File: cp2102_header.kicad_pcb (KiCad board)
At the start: 2 copper layers, 15.2 x 22.9 mm, 32 parts, among them J1 FTDI, J2 USB_B_Micro, J22 USB_B_Micro, J8 mount, Q3 BSS138PS, Q4 BSS138PS, U2 CP2102N

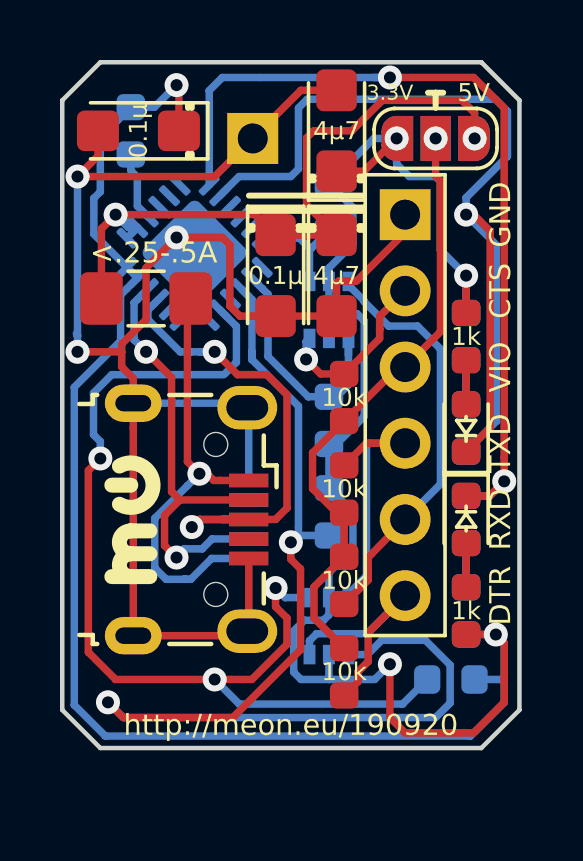
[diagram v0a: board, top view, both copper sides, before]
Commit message: allow for second type of micro usb connector
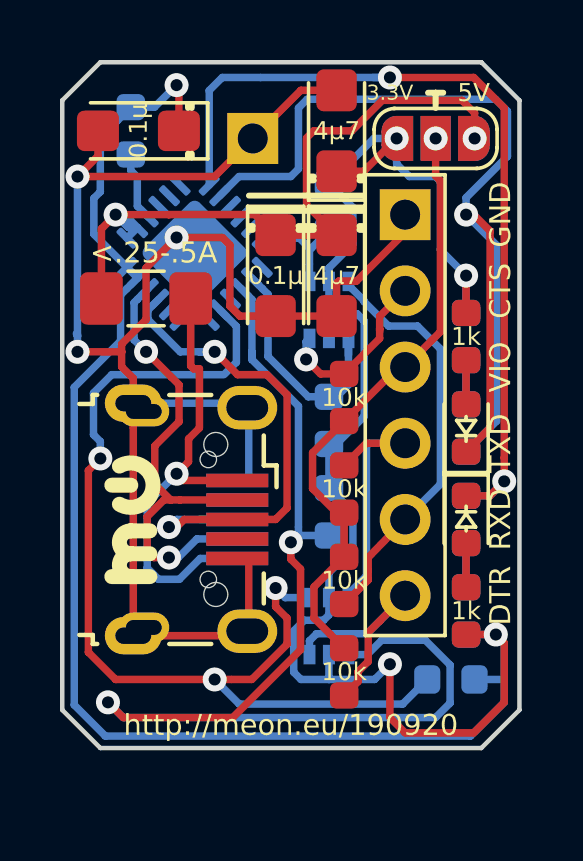
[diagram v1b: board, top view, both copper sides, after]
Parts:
- J2: footprint Connector_USB:USB_Micro-B_Wuerth_629105150521 -> Connector_USB:USB_Micro-B_Wuerth_629105150521_plus_Pitch_7.2mm
- J22: footprint test-footprint:USB_Micro-B_Wuerth_629105150521_usb_lines_only -> Connector_USB:USB_Micro-B_Wuerth_629105150521_plus_Pitch_7.2mm_no_tht
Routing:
- net D-: track 15.2 -> 16.9 mm
- net D+: track 16.9 -> 18.5 mm

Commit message: replace tantalum with ceramic capacitors
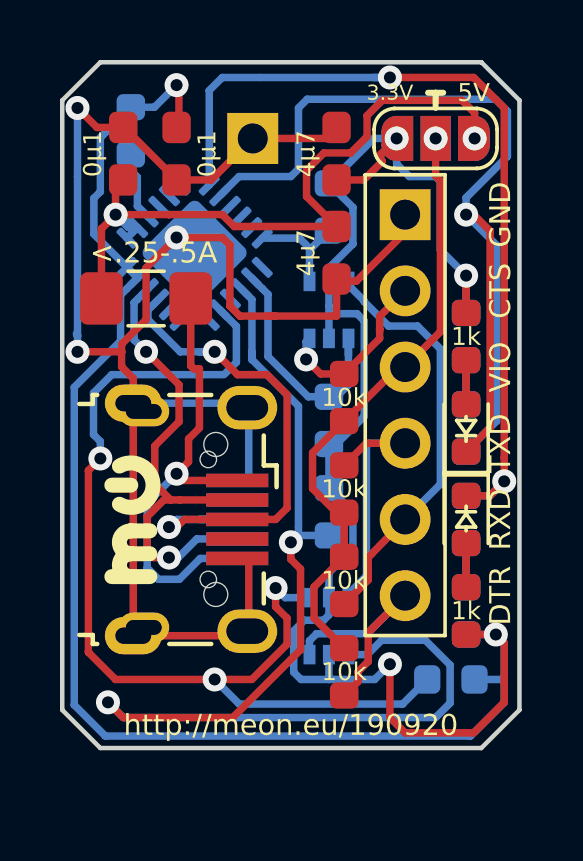
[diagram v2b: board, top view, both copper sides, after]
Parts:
- C21, C23: footprint Capacitor_Tantalum_SMD:CP_EIA-3216-18_Kemet-A -> Capacitor_SMD:C_0603_1608Metric_Pad1.05x0.95mm_HandSolder_no_lines
- C22, C24: value 0.1μ -> 0μ1; footprint Capacitor_Tantalum_SMD:CP_EIA-3216-18_Kemet-A -> Capacitor_SMD:C_0603_1608Metric_Pad1.05x0.95mm_HandSolder_no_lines
- F2: value 0.5A -> .25-.5A
- moved C24 6.51 mm to (79.5, 74.2), turned to 90 degrees
- moved C22 1.48 mm to (81.3, 74.2), turned to 270 degrees
- moved C21 0.76 mm to (86.6, 74.2)
- moved C23 0.76 mm to (86.6, 77.5)
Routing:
- net GND: track 60.7 -> 61.7 mm
- net +5V: track 24.0 -> 24.6 mm

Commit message: compact dimensions
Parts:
- C24: moved to B.Cu
- Q3, R31, R34, R41, R44: moved to F.Cu
- moved C24 12.0 mm to (91.2, 76.7), turned to 270 degrees
- moved R44 8.90 mm to (85.9, 74.2), turned to 180 degrees
- moved R31 7.62 mm to (81.8, 92.2), turned to 180 degrees
- moved Q4 6.23 mm to (86.1, 73.2)
- moved R46 4.77 mm to (91.2, 80.3)
- moved R33 4.77 mm to (91.2, 89.4)
- moved R36 4.77 mm to (91.2, 83.3)
- moved R43 4.77 mm to (91.2, 86.4)
- moved C23 4.64 mm to (91.2, 76.7)
- moved R41 3.34 mm to (85.9, 72.6), turned to 0 degrees
- moved C21 3.25 mm to (88.6, 76.7), turned to 270 degrees
- moved D21 2.54 mm to (88.4, 83.3)
- moved D22 2.54 mm to (88.4, 86.4)
- moved D23 2.54 mm to (88.4, 83.3)
- moved D24 2.54 mm to (88.4, 86.4)
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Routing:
- net U_TXD: track 39.2 -> 17.7 mm, vias 2 -> 1
- net RXD: track 13.9 -> 31.7 mm
- net TXL: track 33.5 -> 18.4 mm, vias 1 -> 3
- net +3V3: track 94.0 -> 80.1 mm
- net GND: track 61.7 -> 74.1 mm, vias 3 -> 2
- net RXL: track 29.3 -> 18.8 mm, vias 2 -> 3
- net CTS: track 5.89 -> 14.9 mm, vias 1 -> 0
- net U_RXD: track 8.37 -> 14.6 mm, vias 0 -> 1
- net U_DTR: track 34.6 -> 28.7 mm, vias 3 -> 1
- net TXD: track 8.97 -> 14.7 mm, vias 0 -> 1
- net U_CTS: track 3.71 -> 9.44 mm, vias 0 -> 1
- net +5V: track 24.6 -> 29.8 mm
- net VIO: track 20.6 -> 24.3 mm
- net D-: track 16.9 -> 19.8 mm
- net DTR: track 8.44 -> 10.1 mm
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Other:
- board size 15.2 x 22.9 mm -> 14.6 x 22.9 mm

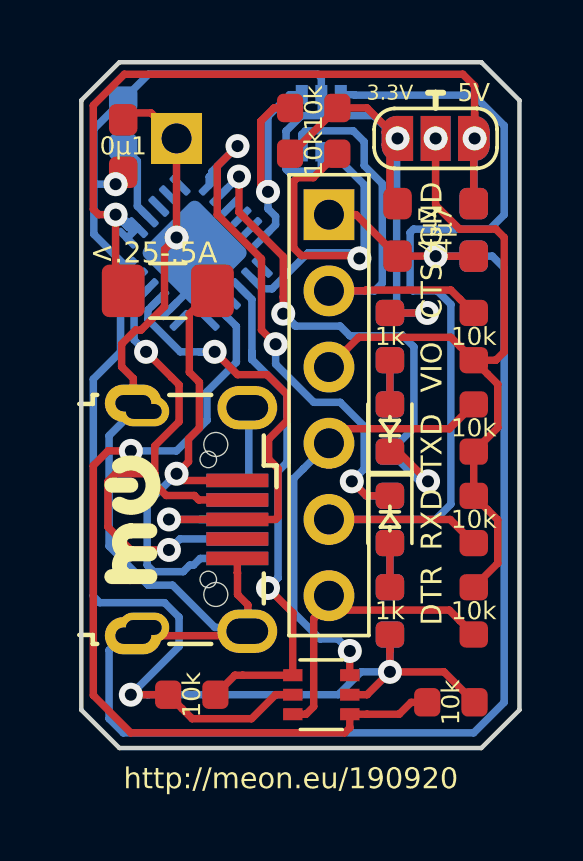
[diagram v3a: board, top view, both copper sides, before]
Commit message: even smaller pcb, only one R per pair of tx/rx leds
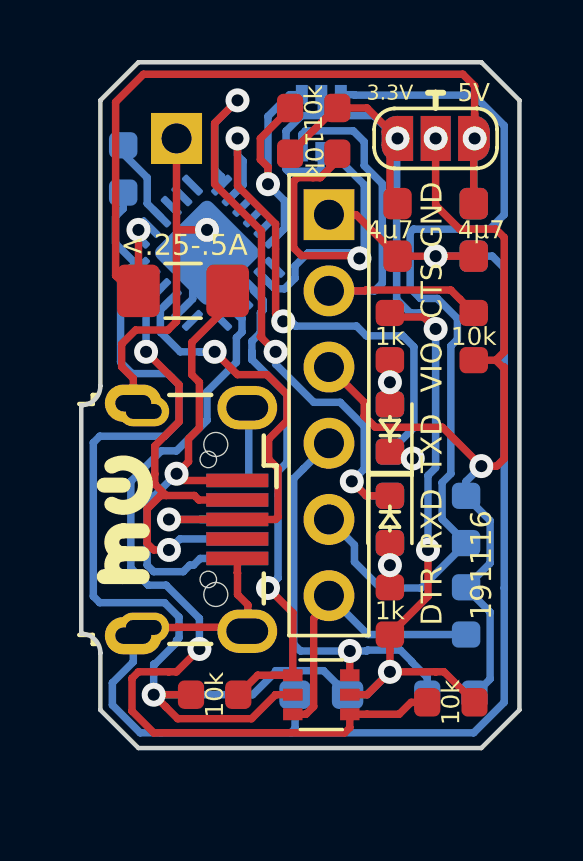
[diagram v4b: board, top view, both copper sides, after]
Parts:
- removed R23, R24: 1k, Resistor_SMD:R_0603_1608Metric
- C22: value 0μ1 -> 0.1μ; moved to B.Cu
- C24: value 0μ1 -> 0.1μ
- R33, R36, R43: moved to B.Cu
- moved C22 19.4 mm to (86.1, 92.2), turned to 180 degrees
- moved R36 8.92 mm to (90.4, 92.2), turned to 0 degrees
- moved R2 1.52 mm to (79.5, 74.7), turned to 270 degrees
- moved R31 0.76 mm to (82.5, 92.2)
- moved F2 0.51 mm to (81.5, 78.7)
- moved U2 0.41 mm to (82.3, 77.5)
- moved R33 0.25 mm to (90.9, 89.4)
- moved R43 0.25 mm to (90.9, 86.4)
- moved REF** 0.25 mm to (79.5, 86.4)
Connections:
- D23 pad 2: Net-(D23-Pad2) -> Net-(D21-Pad2)
- D24 pad 2: Net-(D24-Pad2) -> Net-(D22-Pad2)
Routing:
- net GND: track 74.1 -> 63.3 mm
- net VIO: track 24.3 -> 29.9 mm, vias 1 -> 2
- net RXL: track 18.8 -> 22.0 mm
- net D-: track 19.8 -> 16.9 mm
- net TXL: track 18.4 -> 20.4 mm
- net Net-(D24-Pad2): track 1.47 -> 0.00 mm
- net Net-(D23-Pad2): track 1.47 -> 0.00 mm
- net +3V3: track 80.1 -> 81.5 mm
- net +5V: track 29.8 -> 28.4 mm
- net TXD: track 14.7 -> 13.5 mm
- net RXD: track 31.7 -> 30.6 mm
- net Net-(D22-Pad2): track 1.47 -> 2.24 mm, vias 0 -> 1
- net Net-(D21-Pad2): track 1.47 -> 2.21 mm, vias 0 -> 1
- net U_TXD: track 17.7 -> 17.0 mm
- net U_DTR: track 28.7 -> 29.3 mm
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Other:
- outline, holes or cut-outs redrawn
- board text added: "191116"
- board text removed: "http://meon.eu/190920"

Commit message: use less parts, cp2102 uart inputs are 5V tollerant
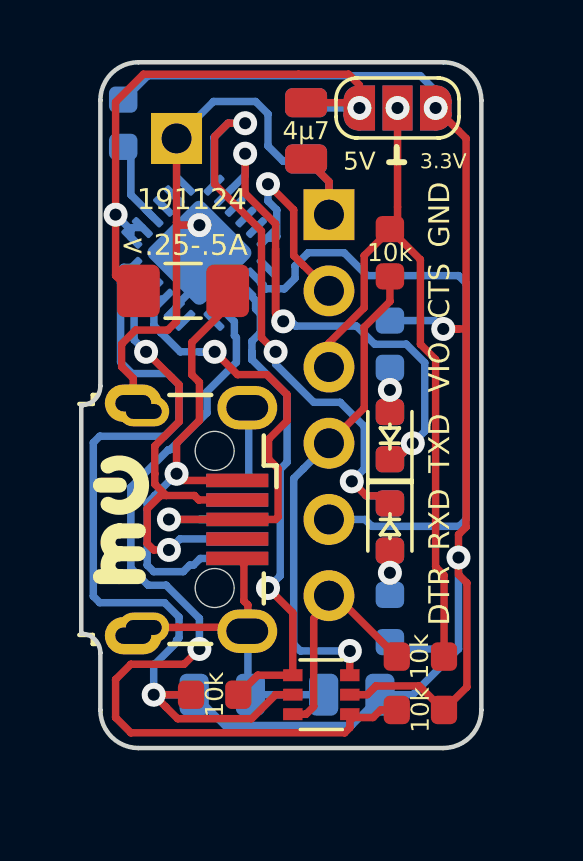
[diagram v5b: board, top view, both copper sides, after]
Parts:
- removed J22: USB_B_Micro, Connector_USB:USB_Micro-B_Wuerth_629105150521_plus_Pitch_7.2mm_no_tht
- removed the JP9 at (89.9, 73.7)
- removed JP92: sjmp, Jumper (GitHub):SolderJumper-3_P1.3mm_Open_RoundedPad1.0x1.5mm_no_arrow
- removed Q4: BSS138PS, Package_TO_SOT_SMD (GitHub):SOT-363_SC-70-6_dot
- removed R41, R43, R44, R46: 10k, Resistor_SMD (GitHub):R_0603_1608Metric_no_lines
- added JP9: SJMP, Jumper (GitHub):SolderJumper-3_P1.3mm_Open_RoundedPad1.0x1.5mm_no_arrow, B.Cu at (88.6, 72.6)
- added JP9: SJMP, Jumper (GitHub):SolderJumper-3_P1.3mm_Open_RoundedPad1.0x1.5mm_no_arrow, F.Cu at (88.6, 72.6)
- C21: footprint Capacitor_SMD:C_0603_1608Metric_Pad1.05x0.95mm_HandSolder_no_lines -> Capacitor_SMD:C_0805_2012Metric_no_lines; moved to B.Cu
- C22, C23, C24: footprint Capacitor_SMD:C_0603_1608Metric_Pad1.05x0.95mm_HandSolder_no_lines -> Capacitor_SMD:C_0805_2012Metric_no_lines
- J1: footprint Connector_PinSocket_2.54mm:PinSocket_1x06_P2.54mm_Vertical_closed -> Connector_PinSocket_2.54mm:PinSocket_1x06_P2.54mm_Vertical_no_lines
- J2: footprint Connector_USB:USB_Micro-B_Wuerth_629105150521_plus_Pitch_7.2mm -> Connector_USB:USB_Micro-B_Wuerth_629105150521_plus_Pitch_7.2mm_doubleside
- R21, R22: moved to B.Cu
- R33, R36: moved to F.Cu
- moved C21 15.6 mm to (87.1, 92.2), turned to 180 degrees
- moved R36 14.9 mm to (88.4, 77.5), turned to 90 degrees
- moved C23 6.49 mm to (85.6, 73.4)
- moved C24 6.49 mm to (85.6, 73.4)
- moved C22 3.30 mm to (82.8, 92.2), turned to 0 degrees
- moved R33 2.16 mm to (89.4, 90.9), turned to 0 degrees
- moved R2 1.52 mm to (79.5, 73.2), turned to 90 degrees
- moved R34 1.05 mm to (89.4, 92.7)
- moved D21 0.25 mm to (88.4, 83.6)
- moved D22 0.25 mm to (88.4, 86.6)
- moved D23 0.25 mm to (88.4, 83.6)
- moved D24 0.25 mm to (88.4, 86.6)
- moved R21 0.25 mm to (88.4, 80.5)
- moved R22 0.25 mm to (88.4, 89.7)
- moved U2 0.25 mm to (82.0, 77.5)
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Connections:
- J2 pad 4: (no net) -> Net-(J2-Pad4)
- U2 pad 18: U_CTS -> CTS
- U2 pad 20: U_RXD -> RXD
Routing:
- net GND: track 63.3 -> 38.7 mm, vias 2 -> 1
- net U_RXD: track 14.7 -> 0.00 mm, vias 1 -> 0
- net RXD: track 30.6 -> 20.7 mm
- net U_CTS: track 8.88 -> 0.00 mm, vias 1 -> 0
- net CTS: track 14.9 -> 6.62 mm, vias 0 -> 1
- net +5V: track 28.4 -> 21.4 mm
- net VIO: track 29.9 -> 24.6 mm, vias 2 -> 1
- net +3V3: track 81.5 -> 85.1 mm, vias 5 -> 4
- net TXD: track 13.5 -> 16.4 mm
- net DTR: track 9.82 -> 8.04 mm
- net TXL: track 20.4 -> 21.5 mm
- net RXL: track 22.0 -> 21.2 mm
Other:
- board size 14.6 x 22.9 mm -> 13.3 x 22.9 mm
- board text added: "191124"
- board text added: "meon.eu/191124"
- board text removed: "191116"

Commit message: more space for cp2102n, move capacitor away from header pin
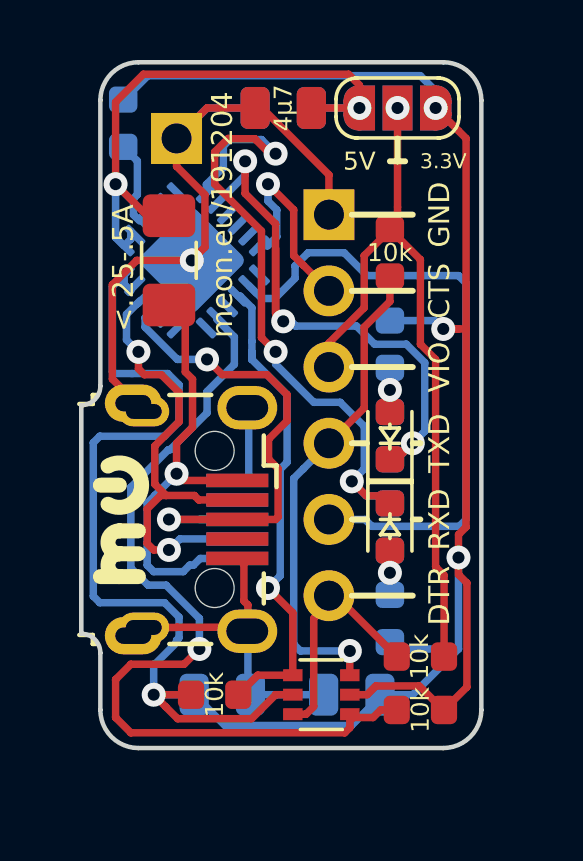
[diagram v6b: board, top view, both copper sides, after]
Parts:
- moved F2 1.12 mm to (81.0, 77.7), turned to 270 degrees
- moved C23 1.08 mm to (84.8, 72.6), turned to 180 degrees
- moved C24 1.08 mm to (84.8, 72.6), turned to 180 degrees
- moved U2 0.36 mm to (81.8, 77.7)
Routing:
- net GND: track 38.7 -> 41.4 mm
- net RXL: track 21.2 -> 22.9 mm
- net RXD: track 20.7 -> 21.4 mm
- net +5V: track 21.4 -> 20.9 mm
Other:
- board text added: "meon.eu/191204"
- board text removed: "191124"
- board text removed: "meon.eu/191124"
